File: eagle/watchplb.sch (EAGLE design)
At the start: 94 parts, among them IC1 SAM-M8Q, IC2 BM70BLES1FC2-0B03AA, Q1 8MHz / LFXTAL020423Reel, Q2 DMT5015LFDF, U1 MCP111-XXXXX/TO, U2 STM32L073RZ, U3 MCP2200-I/SS

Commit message: added mouser numbers for most products, changed switches to smd
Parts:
- added BTN_1, BTN_2, BTN_3, BTN_4, BTN_NRST: PTR1B2,54, testpad:PTR1B2,54
- LED1: value (none) -> BLUE
- S1, S2, S3, S4, S5: device switch-omron:10-XX -> Hick:TL3305
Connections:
- net BTN_1: now also BTN_1.TP
- net BTN_2: now also BTN_2.TP
- net BTN_3: now also BTN_3.TP
- net BTN_4: now also BTN_4.TP
- net NRST: now also BTN_NRST.TP
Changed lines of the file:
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@@
 <part name="GND4" library="supply1" deviceset="GND" device=""/>
 <part name="+3V5" library="supply1" deviceset="+3V3" device=""/>
-<part name="LED1" library="adafruit" deviceset="LED" device="CHIP-LED0805"/>
+<part name="LED1" library="adafruit" deviceset="LED" device="CHIP-LED0805" value="BLUE"/>
 <part name="+3V6" library="supply1" deviceset="+3V3" device=""/>
 <part name="CONFIG_INTERFACE_TEST_POINT" library="pinhead" deviceset="PINHD-1X5" device=""/>
@@
 <part name="GND11" library="supply1" deviceset="GND" device=""/>
 <part name="C10" library="resistor" deviceset="C-EU" device="C0805" value="1uF"/>
-<part name="S1" library="switch-omron" deviceset="10-XX" device=""/>
+<part name="S1" library="Hick" deviceset="TL3305" device=""/>
 <part name="C11" library="resistor" deviceset="C-EU" device="C0805" value="100nF"/>
 <part name="R4" library="resistor" deviceset="R-EU_" device="M0805" value="47k"/>
 <part name="GND12" library="supply1" deviceset="GND" device=""/>
 <part name="+3V14" library="supply1" deviceset="+3V3" device=""/>
-<part name="S2" library="switch-omron" deviceset="10-XX" device=""/>
+<part name="S2" library="Hick" deviceset="TL3305" device=""/>
 <part name="R6" library="resistor" deviceset="R-EU_" device="M0805" value="10k"/>
 <part name="R7" library="resistor" deviceset="R-EU_" device="M0805" value="10k"/>
 <part name="C12" library="resistor" deviceset="C-EU" device="C0805" value="100nF"/>
 <part name="+3V15" library="supply1" deviceset="+3V3" device=""/>
-<part name="S3" library="switch-omron" deviceset="10-XX" device=""/>
+<part name="S3" library="Hick" deviceset="TL3305" device=""/>
 <part name="R5" library="resistor" deviceset="R-EU_" device="M0805" value="10k"/>
 <part name="R8" library="resistor" deviceset="R-EU_" device="M0805" value="10k"/>
@@
 <part name="R11" library="resistor" deviceset="R-EU_" device="M0805" value="220R"/>
 <part name="GND18" library="supply1" deviceset="GND" device=""/>
-<part name="S4" library="switch-omron" deviceset="10-XX" device=""/>
+<part name="S4" library="Hick" deviceset="TL3305" device=""/>
 <part name="R12" library="resistor" deviceset="R-EU_" device="M0805" value="10k"/>
 <part name="R13" library="resistor" deviceset="R-EU_" device="M0805" value="10k"/>
@@
 <part name="R15" library="resistor" deviceset="R-EU_" device="M0805" value="220R"/>
 <part name="U3" library="MCP2200-iSS" deviceset="MCP2200-I/SS" device=""/>
-<part name="S5" library="switch-omron" deviceset="10-XX" device=""/>
+<part name="S5" library="Hick" deviceset="TL3305" device=""/>
 <part name="R16" library="resistor" deviceset="R-EU_" device="M0805" value="10k"/>
 <part name="R17" library="resistor" deviceset="R-EU_" device="M0805" value="10k"/>
@@
 <part name="D4" library="adafruit" deviceset="DIODE" device="SOD-123"/>
 <part name="D5" library="adafruit" deviceset="DIODE" device="SOD-123"/>
+<part name="BTN_1" library="testpad" deviceset="PTR1" device="B2,54"/>
+<part name="BTN_2" library="testpad" deviceset="PTR1" device="B2,54"/>
+<part name="BTN_3" library="testpad" deviceset="PTR1" device="B2,54"/>
+<part name="BTN_4" library="testpad" deviceset="PTR1" device="B2,54"/>
+<part name="BTN_NRST" library="testpad" deviceset="PTR1" device="B2,54"/>
 </parts>
 <sheets>
@@
 <instance part="D4" gate="G$1" x="601.98" y="88.9" rot="R180"/>
 <instance part="D5" gate="G$1" x="601.98" y="83.82" rot="R180"/>
+<instance part="BTN_1" gate="G$1" x="589.28" y="152.4" smashed="yes" rot="R180">
+<attribute name="NAME" x="590.55" y="158.75" size="1.778" layer="95" rot="R90"/>
+<attribute name="TP_SIGNAL_NAME" x="588.01" y="154.94" size="1.778" layer="97" rot="R180"/>
+</instance>
+<instance part="BTN_2" gate="G$1" x="627.38" y="152.4" smashed="yes" rot="R180">
+<attribute name="NAME" x="628.65" y="158.75" size="1.778" layer="95" rot="R90"/>
+<attribute name="TP_SIGNAL_NAME" x="626.11" y="154.94" size="1.778" layer="97" rot="R180"/>
+</instance>
+<instance part="BTN_3" gate="G$1" x="665.48" y="152.4" smashed="yes" rot="R180">
+<attribute name="NAME" x="666.75" y="158.75" size="1.778" layer="95" rot="R90"/>
+<attribute name="TP_SIGNAL_NAME" x="664.21" y="154.94" size="1.778" layer="97" rot="R180"/>
+</instance>
+<instance part="BTN_4" gate="G$1" x="703.58" y="152.4" smashed="yes" rot="R180">
+<attribute name="NAME" x="704.85" y="158.75" size="1.778" layer="95" rot="R90"/>
+<attribute name="TP_SIGNAL_NAME" x="702.31" y="154.94" size="1.778" layer="97" rot="R180"/>
+</instance>
+<instance part="BTN_NRST" gate="G$1" x="739.14" y="152.4" smashed="yes" rot="R180">
+<attribute name="NAME" x="740.41" y="158.75" size="1.778" layer="95" rot="R90"/>
+<attribute name="TP_SIGNAL_NAME" x="737.87" y="154.94" size="1.778" layer="97" rot="R180"/>
+</instance>
 </instances>
 <busses>
@@
 <wire x1="622.3" y1="152.4" x2="622.3" y2="154.94" width="0.1524" layer="91"/>
 <junction x="619.76" y="152.4"/>
-<wire x1="619.76" y1="149.86" x2="635" y2="149.86" width="0.1524" layer="91"/>
+<wire x1="619.76" y1="149.86" x2="627.38" y2="149.86" width="0.1524" layer="91"/>
 <label x="627.38" y="149.86" size="1.778" layer="95"/>
+<pinref part="BTN_2" gate="G$1" pin="TP"/>
+<wire x1="627.38" y1="149.86" x2="635" y2="149.86" width="0.1524" layer="91"/>
+<junction x="627.38" y="149.86"/>
 </segment>
 <segment>
@@
 <wire x1="584.2" y1="152.4" x2="584.2" y2="154.94" width="0.1524" layer="91"/>
 <junction x="581.66" y="152.4"/>
-<wire x1="581.66" y1="149.86" x2="596.9" y2="149.86" width="0.1524" layer="91"/>
+<wire x1="581.66" y1="149.86" x2="589.28" y2="149.86" width="0.1524" layer="91"/>
 <label x="589.28" y="149.86" size="1.778" layer="95"/>
+<pinref part="BTN_1" gate="G$1" pin="TP"/>
+<wire x1="589.28" y1="149.86" x2="596.9" y2="149.86" width="0.1524" layer="91"/>
+<junction x="589.28" y="149.86"/>
 </segment>
 <segment>
@@
 <wire x1="718.82" y1="144.78" x2="718.82" y2="149.86" width="0.1524" layer="91"/>
 <wire x1="718.82" y1="149.86" x2="734.06" y2="149.86" width="0.1524" layer="91"/>
-<wire x1="746.76" y1="149.86" x2="736.6" y2="149.86" width="0.1524" layer="91"/>
+<wire x1="746.76" y1="149.86" x2="739.14" y2="149.86" width="0.1524" layer="91"/>
 <junction x="736.6" y="149.86"/>
 <label x="739.14" y="149.86" size="1.778" layer="95"/>
+<pinref part="BTN_NRST" gate="G$1" pin="TP"/>
+<wire x1="739.14" y1="149.86" x2="736.6" y2="149.86" width="0.1524" layer="91"/>
+<junction x="739.14" y="149.86"/>
 </segment>
 <segment>
@@
 <wire x1="660.4" y1="152.4" x2="660.4" y2="154.94" width="0.1524" layer="91"/>
 <junction x="657.86" y="152.4"/>
-<wire x1="657.86" y1="149.86" x2="673.1" y2="149.86" width="0.1524" layer="91"/>
+<wire x1="657.86" y1="149.86" x2="665.48" y2="149.86" width="0.1524" layer="91"/>
 <label x="665.48" y="149.86" size="1.778" layer="95"/>
+<pinref part="BTN_3" gate="G$1" pin="TP"/>
+<wire x1="665.48" y1="149.86" x2="673.1" y2="149.86" width="0.1524" layer="91"/>
+<junction x="665.48" y="149.86"/>
 </segment>
 <segment>
@@
 <wire x1="698.5" y1="152.4" x2="698.5" y2="154.94" width="0.1524" layer="91"/>
 <junction x="695.96" y="152.4"/>
-<wire x1="695.96" y1="149.86" x2="711.2" y2="149.86" width="0.1524" layer="91"/>
+<wire x1="695.96" y1="149.86" x2="703.58" y2="149.86" width="0.1524" layer="91"/>
 <label x="703.58" y="149.86" size="1.778" layer="95"/>
-</segment>
-<segment>
+<pinref part="BTN_4" gate="G$1" pin="TP"/>
+<wire x1="703.58" y1="149.86" x2="711.2" y2="149.86" width="0.1524" layer="91"/>
+<junction x="703.58" y="149.86"/>
+</segment>
+<segment>

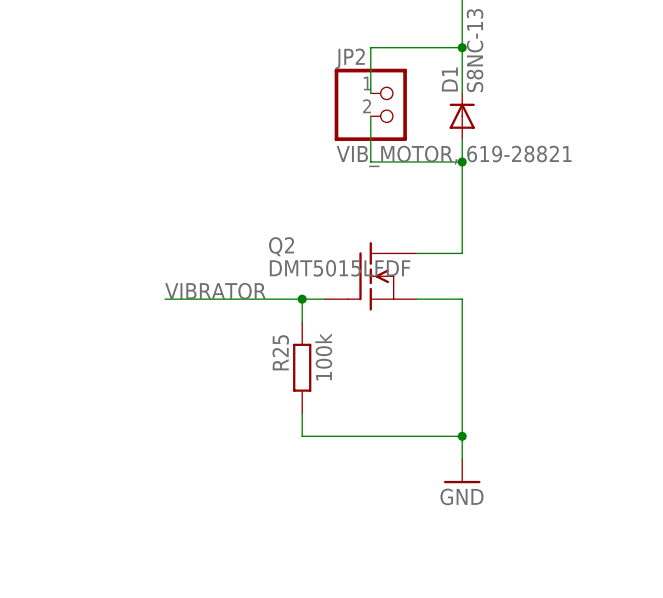
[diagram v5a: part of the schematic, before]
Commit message: changed mosfet to one with sot23 footprint
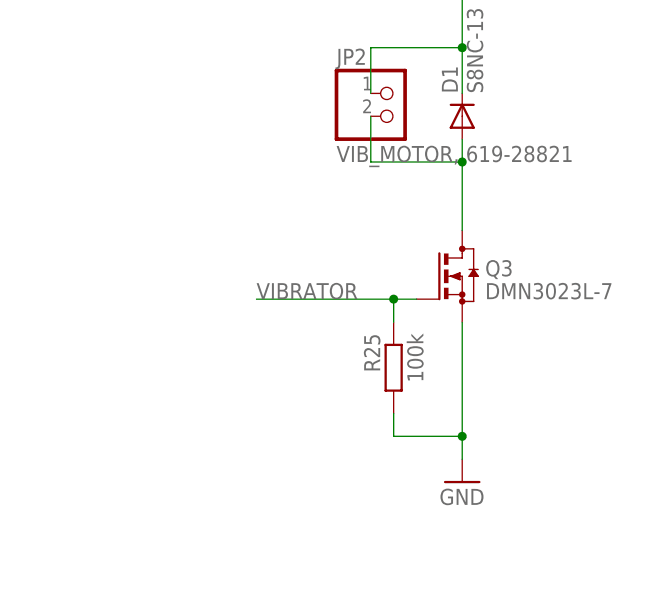
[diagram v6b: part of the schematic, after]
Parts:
- removed Q2: DMT5015LFDF, Hick:DMT5015LFDF
- added Q3: DMN3023L-7, transistor-small-signal:BSS123
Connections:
- net GND: now also Q3.S; no longer Q2.S
- net N$28: now also Q3.D; no longer Q2.D
- net VIBRATOR: now also Q3.G; no longer Q2.G
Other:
- moved on the sheet: R25
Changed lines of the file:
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@@
 <part name="D1" library="diode" deviceset="DIODE-" device="SMC" value="S8NC-13 "/>
 <part name="P+2" library="supply1" deviceset="V+" device=""/>
-<part name="Q2" library="Hick" deviceset="DMT5015LFDF" device=""/>
 <part name="GND25" library="supply1" deviceset="GND" device=""/>
 <part name="R25" library="resistor" deviceset="R-EU_" device="M0805" value="100k"/>
@@
 <part name="BTN_4" library="testpad" deviceset="PTR1" device="B2,54"/>
 <part name="BTN_NRST" library="testpad" deviceset="PTR1" device="B2,54"/>
+<part name="Q3" library="transistor-small-signal" deviceset="BSS123" device="" value="DMN3023L-7 "/>
 </parts>
 <sheets>
@@
 <instance part="D1" gate="G$1" x="772.16" y="86.36" rot="R90"/>
 <instance part="P+2" gate="1" x="772.16" y="104.14"/>
-<instance part="Q2" gate="G$1" x="762" y="68.58"/>
 <instance part="GND25" gate="1" x="772.16" y="45.72"/>
-<instance part="R25" gate="G$1" x="754.38" y="58.42" rot="MR270"/>
+<instance part="R25" gate="G$1" x="764.54" y="58.42" rot="MR270"/>
 <instance part="VIBR" gate="G$1" x="195.58" y="287.02" smashed="yes" rot="R90">
 <attribute name="NAME" x="201.93" y="286.258" size="1.778" layer="95"/>
@@
 <attribute name="TP_SIGNAL_NAME" x="737.87" y="154.94" size="1.778" layer="97" rot="R180"/>
 </instance>
+<instance part="Q3" gate="G$1" x="772.16" y="68.58"/>
 </instances>
 <busses>
@@
 </segment>
 <segment>
-<pinref part="Q2" gate="G$1" pin="S"/>
-<wire x1="767.08" y1="66.04" x2="772.16" y2="66.04" width="0.1524" layer="91"/>
-<wire x1="772.16" y1="66.04" x2="772.16" y2="50.8" width="0.1524" layer="91"/>
+<wire x1="772.16" y1="63.5" x2="772.16" y2="50.8" width="0.1524" layer="91"/>
 <pinref part="GND25" gate="1" pin="GND"/>
 <pinref part="R25" gate="G$1" pin="2"/>
 <wire x1="772.16" y1="50.8" x2="772.16" y2="48.26" width="0.1524" layer="91"/>
-<wire x1="754.38" y1="53.34" x2="754.38" y2="50.8" width="0.1524" layer="91"/>
-<wire x1="754.38" y1="50.8" x2="772.16" y2="50.8" width="0.1524" layer="91"/>
+<wire x1="764.54" y1="53.34" x2="764.54" y2="50.8" width="0.1524" layer="91"/>
+<wire x1="764.54" y1="50.8" x2="772.16" y2="50.8" width="0.1524" layer="91"/>
 <junction x="772.16" y="50.8"/>
+<pinref part="Q3" gate="G$1" pin="S"/>
 </segment>
 </net>
@@
 <wire x1="762" y1="81.28" x2="772.16" y2="81.28" width="0.1524" layer="91"/>
 <wire x1="772.16" y1="81.28" x2="772.16" y2="83.82" width="0.1524" layer="91"/>
-<pinref part="Q2" gate="G$1" pin="D"/>
-<wire x1="767.08" y1="71.12" x2="772.16" y2="71.12" width="0.1524" layer="91"/>
-<wire x1="772.16" y1="71.12" x2="772.16" y2="81.28" width="0.1524" layer="91"/>
+<wire x1="772.16" y1="73.66" x2="772.16" y2="81.28" width="0.1524" layer="91"/>
 <junction x="772.16" y="81.28"/>
+<pinref part="Q3" gate="G$1" pin="D"/>
 </segment>
 </net>
@@
 <net name="VIBRATOR" class="0">
 <segment>
-<pinref part="Q2" gate="G$1" pin="G"/>
 <pinref part="R25" gate="G$1" pin="1"/>
-<wire x1="756.92" y1="66.04" x2="754.38" y2="66.04" width="0.1524" layer="91"/>
-<wire x1="754.38" y1="66.04" x2="754.38" y2="63.5" width="0.1524" layer="91"/>
-<wire x1="754.38" y1="66.04" x2="739.14" y2="66.04" width="0.1524" layer="91"/>
-<junction x="754.38" y="66.04"/>
-<label x="739.14" y="66.04" size="1.778" layer="95"/>
-</segment>
-<segment>
+<wire x1="767.08" y1="66.04" x2="764.54" y2="66.04" width="0.1524" layer="91"/>
+<wire x1="764.54" y1="66.04" x2="764.54" y2="63.5" width="0.1524" layer="91"/>
+<wire x1="764.54" y1="66.04" x2="749.3" y2="66.04" width="0.1524" layer="91"/>
+<junction x="764.54" y="66.04"/>
+<label x="749.3" y="66.04" size="1.778" layer="95"/>
+<pinref part="Q3" gate="G$1" pin="G"/>
+</segment>
+<segment>

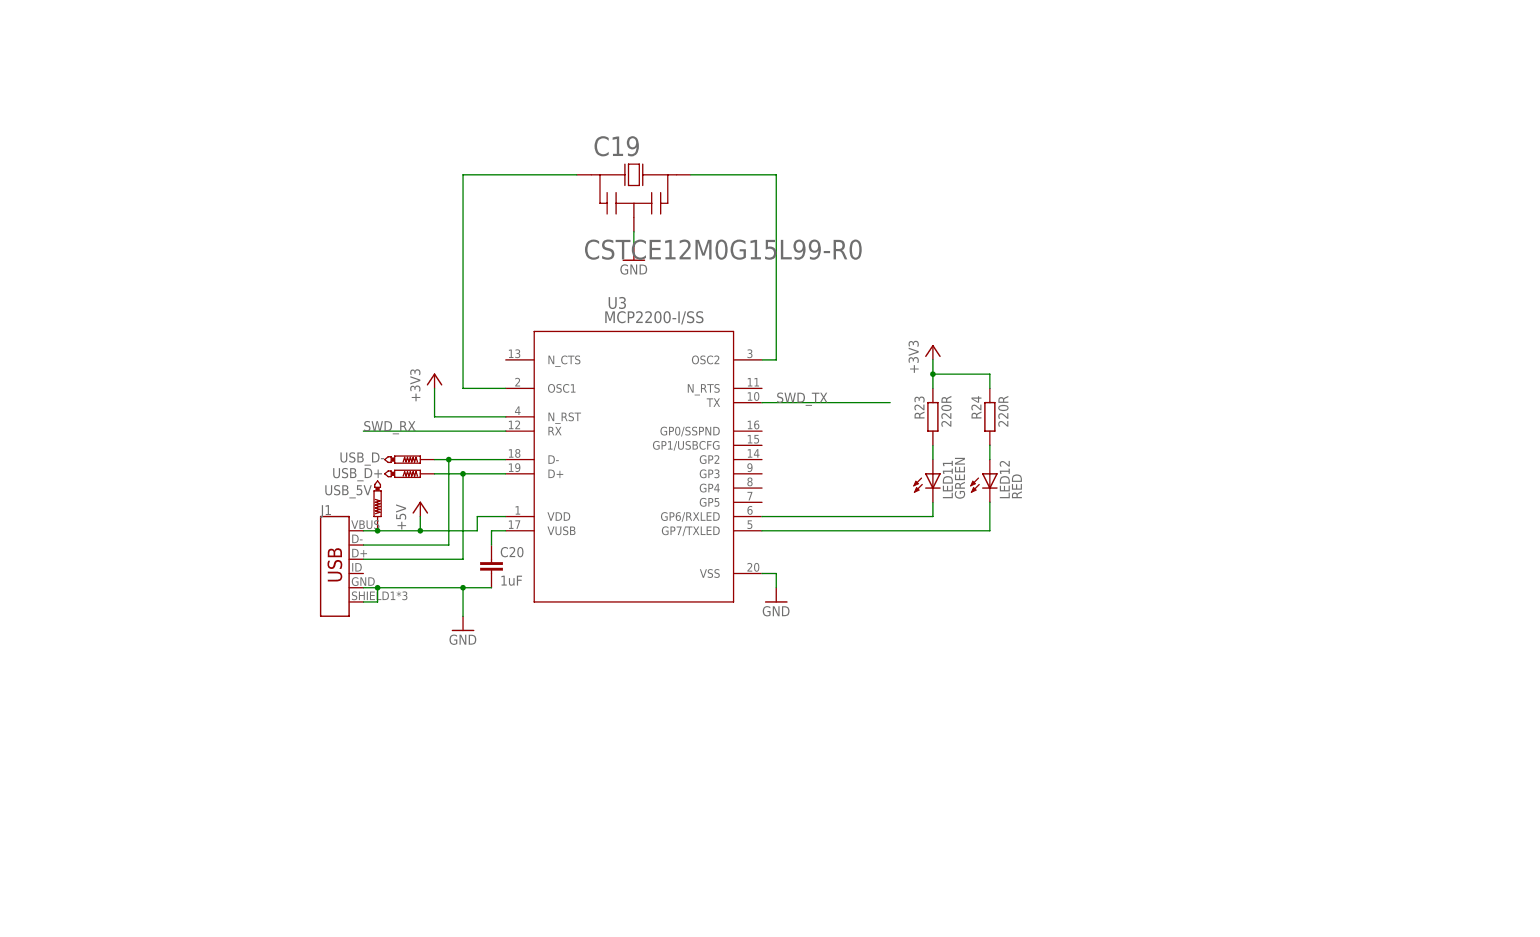
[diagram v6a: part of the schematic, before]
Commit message: added VCOM usb port with protection
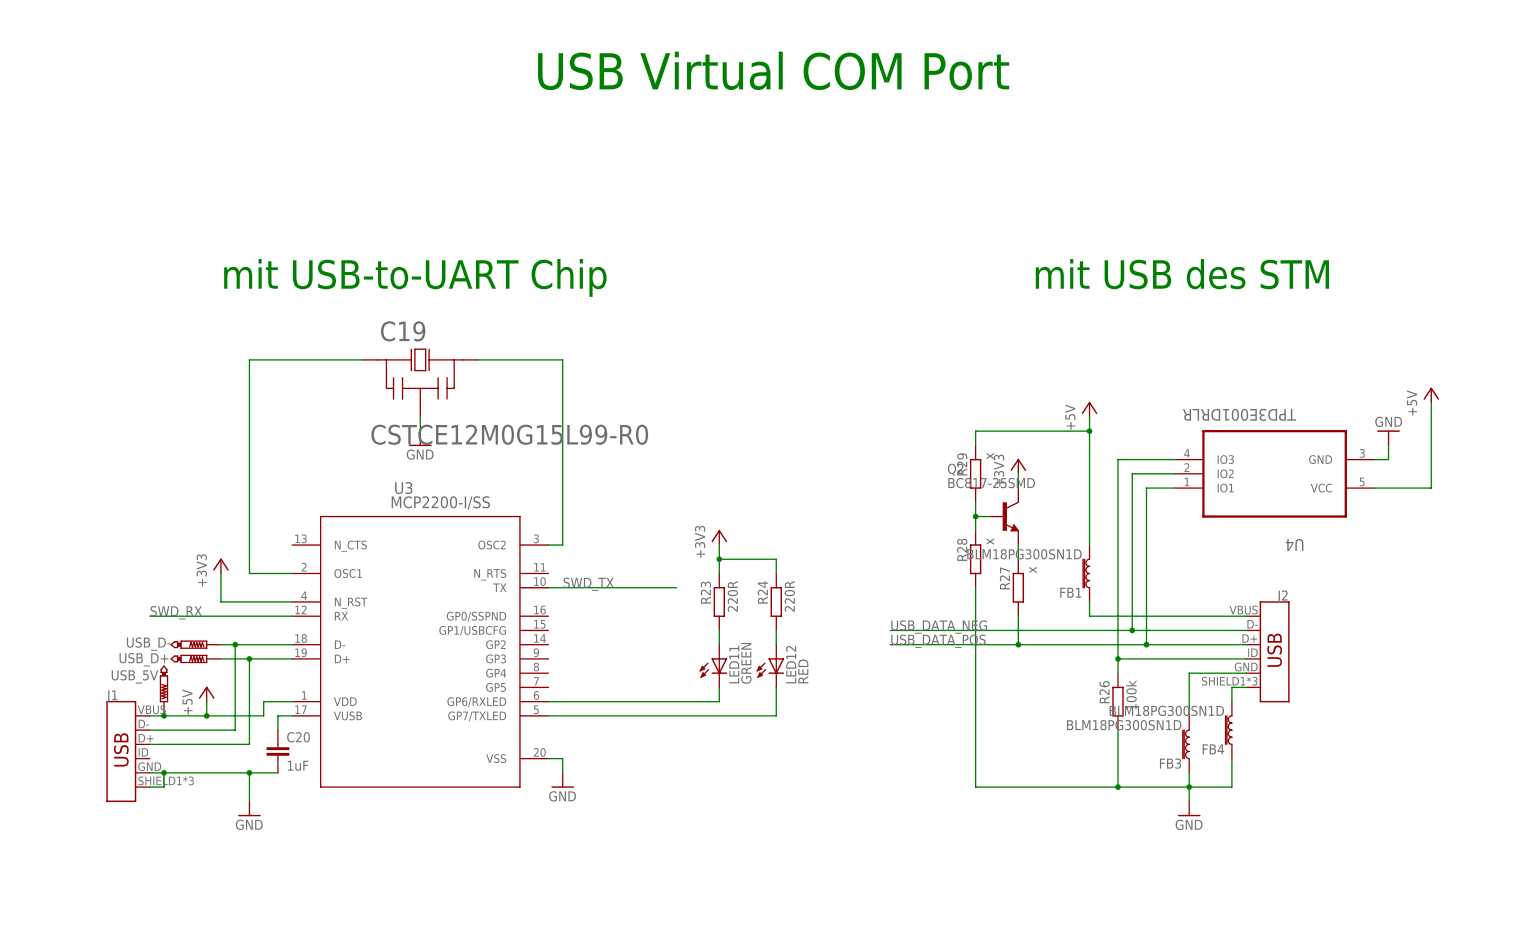
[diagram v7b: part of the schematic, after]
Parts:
- added FB1, FB3, FB4: BLM18PG300SN1D, SparkFun-Coils:FERRITE_BEAD-0603
- added J2: (no value), SparkFun-Connectors:USB_MICRO-B_FEMALE-SMT
- added Q2: BC817-25SMD, transistor-npn:BC817-25SMD
- added R26: 100k, resistor:R-EU_M0805
- added R27, R28, R29: x, resistor:R-EU_M0805
- added U4: TPD3E001DRLR, Texas Instruments_By_element14_Batch_1:TPD3E001DRLR
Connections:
- new net N$29: FB4.2, J2.SHIELD
- new net N$30: FB3.2, J2.GND
- new net N$31: FB1.1, J2.VBUS
- new net N$32: J2.ID, R26.1, U4.IO3
- new net N$35: Q2.E, R27.1
- new net N$36: Q2.B, R28.1, R29.2
- new net USB_DATA_NEG: J2.D-, U4.IO2
- new net USB_DATA_POS: J2.D+, R27.2, U4.IO1
- net +3V3: now also Q2.C
- net +5V: now also FB1.2, R29.1, U4.VCC
- net GND: now also FB3.1, FB4.1, R26.2, R28.2, U4.GND
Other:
- note added: "USB Virtual COM Port"
- note added: "mit USB des STM"
- note added: "mit USB-to-UART Chip"
- moved on the sheet: C19, C20, J1, LED11, LED12, R23, R24, U3, USB_5V, USB_D+, USB_D-

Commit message: added RF transmitter (amp still missing) and generated new pdf of schematic for tobi
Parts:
- added C21, C22, C23, C24: 100nF, resistor:C-EUC0805
- added C25, C26: 27pF, resistor:C-EUC0805
- added C27: 1uF, resistor:C-EUC0805
- added C28, C29, C30, C31, C32, C33, C34, C35, C36, C37: (no value), resistor:C-EUC0805
- added L1, L2, L3, L4, L5, L6, L7: INDUCTOR-0805-3.3UH, SparkFun-Coils:INDUCTOR-0805-3.3UH
- added Q4: 16MHz_LFXTAL051370Reel, adafruit:CRYSTALHC49UP
- added RF_SYSCLK, SPI2_CLK, SPI2_IRQ, SPI2_MISO, SPI2_MOSI, SPI2_SEL_RFTX: PTR1B2,54, testpad:PTR1B2,54
- added U$1: AX5031, Hick:AX5031
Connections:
- new net INT_POWER: C21.2, C22.2, C23.2, C25.2, C26.2, C27.2, C29.2, C30.1, L2.1, L3.2, U$1.VDD1, U$1.VDD2, U$1.VREG
- new net N$33: Q4.2, U$1.CLOCK16P
- new net N$34: Q4.1, U$1.CLOCK16N
- new net N$37: RF_SYSCLK.TP, U$1.SYSCLK
- new net N$38: C24.2, U$1.VDD_IO
- new net N$39: C28.1, L4.1
- new net N$40: C31.1, L1.1
- new net N$41: C29.1, L1.2, L2.2, U$1.ANTN
- new net N$42: C31.2, C32.2, C34.2, L6.1
- new net N$43: C28.2, C33.1, C35.2, L5.2
- new net N$44: C30.2, L3.1, L4.2, U$1.ANTP
- new net N$45: C35.1, C36.2, L6.2, L7.1
- new net RF_SIGNAL: C37.2, L7.2
- new net SPI2_CLK: SPI2_CLK.TP, U$1.CLK, U2.PB10
- new net SPI2_IRQ: SPI2_IRQ.TP, U$1.IRQ, U2.PC0
- new net SPI2_MISO: SPI2_MISO.TP, U$1.MISO_SDO, U2.PC2
- new net SPI2_MOSI: SPI2_MOSI.TP, U$1.MOSI_SDI, U2.PC3
- new net SPI2_SEL_RFTX: SPI2_SEL_RFTX.TP, U$1.SEL, U2.PC1
- net GND: now also C21.1, C22.1, C23.1, C24.1, C25.1, C26.1, C27.1, C32.1, C33.2, C34.1, C36.1, C37.1, L5.1, U$1.GND_PAD
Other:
- note added: "caps for crysta integrated in chip"
- moved on the sheet: NRST_MCU
